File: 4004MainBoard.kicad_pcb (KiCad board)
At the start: 2 copper layers, 95.1 x 72.1 mm, 157 parts, among them J1 BUS, J2 P0 RAM1, J3 CMRAM RAM2, J4 P0 RAM2, J5 DC 5V, Q1 2SA1162GR, Q10 2SC2712GR, Q11 2SA1162GR, Q2 2SC2712GR, Q3 2SA1162GR, Q4 2SC2712GR, Q5 2SA1162GR, Q6 2SA1162GR, Q7 2SA1162GR, Q8 2SA1162GR, Q9 2SC2712GR, SW1 TEST, SW2 RESET, SW3 POWER, U1 74HC08, U2 74HC161, U3 PST600, U4 Intel4004, U5 LT1931A, U6 74LS540, U7 Intel4002-1, U8 Intel4002-1, U9 LT1763, Y1 DLO555MB

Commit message: migrate to KiCad 7
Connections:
- U1 pad 3: Net-(U1-Pad3) -> unconnected-(U1-Pad3)
- U1 pad 6: Net-(U1-Pad6) -> unconnected-(U1-Pad6)
- U2 pad 13: Net-(U2-Pad13) -> unconnected-(U2-Q1-Pad13)
- U2 pad 14: Net-(U2-Pad14) -> unconnected-(U2-Q0-Pad14)
- U2 pad 15: Net-(U2-Pad15) -> unconnected-(U2-Tc-Pad15)
- U2 pad 3: Net-(U2-Pad3) -> unconnected-(U2-P0-Pad3)
- U2 pad 4: Net-(U2-Pad4) -> unconnected-(U2-P1-Pad4)
- U2 pad 5: Net-(U2-Pad5) -> unconnected-(U2-P2-Pad5)
- U2 pad 6: Net-(U2-Pad6) -> unconnected-(U2-P3-Pad6)
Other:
- net class Default removed

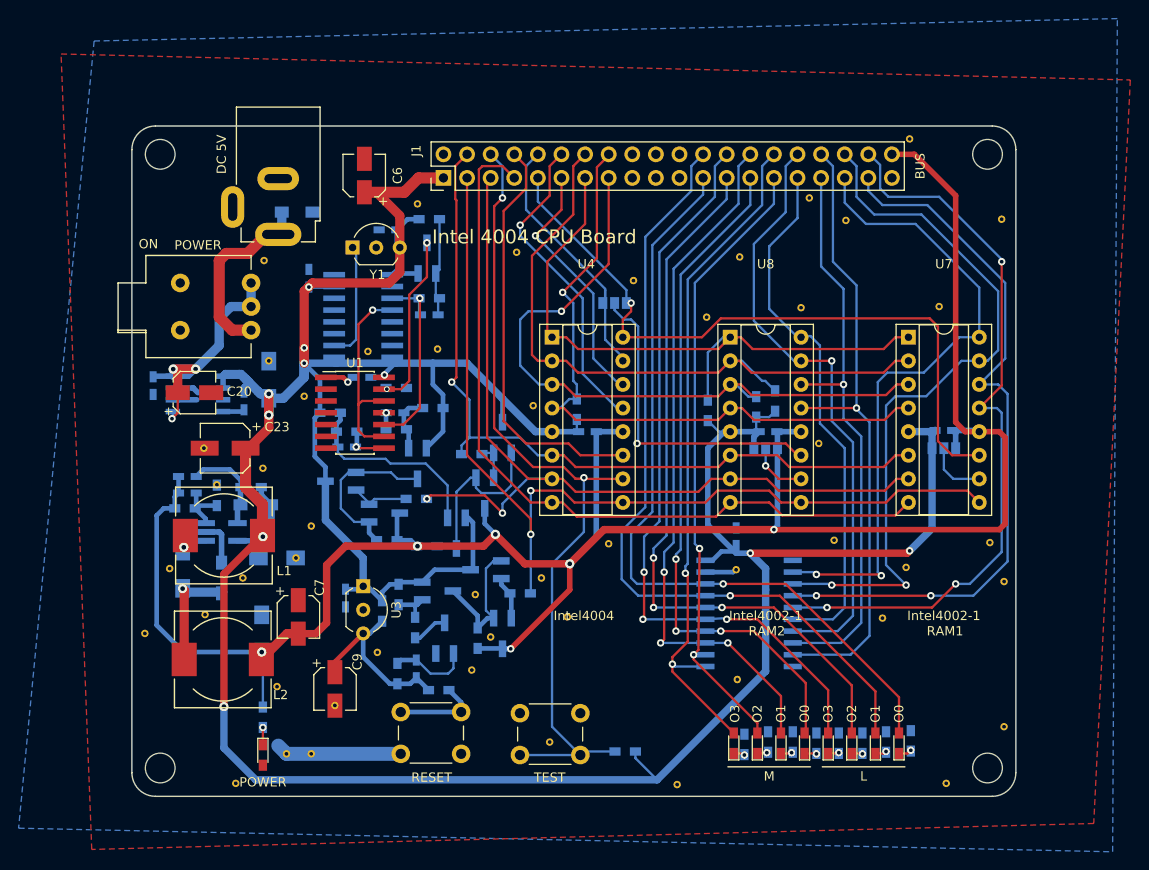
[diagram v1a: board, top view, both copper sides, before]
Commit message: update descrete buffer add notes
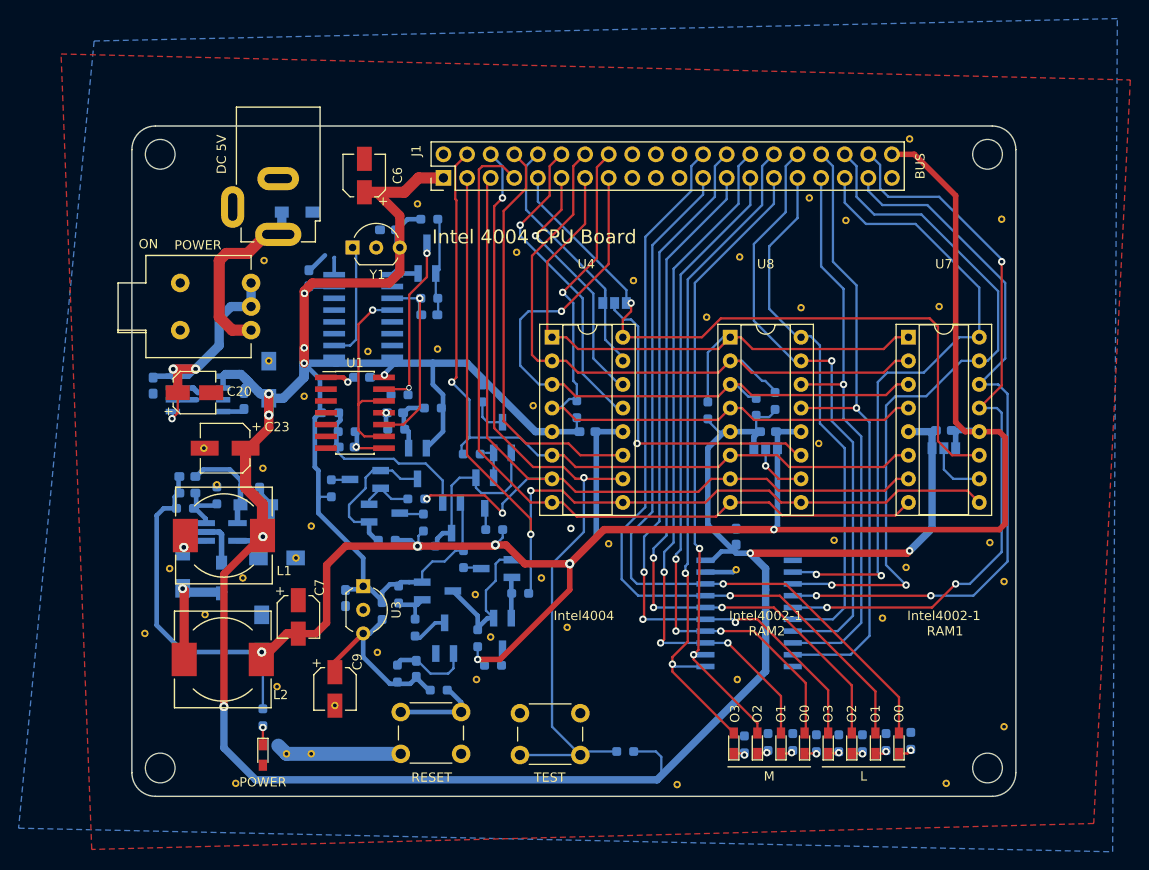
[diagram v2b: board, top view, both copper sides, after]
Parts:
- removed the REF** at (176.4, 137.4)
- added R36: 22, Resistor_SMD:R_0603_1608Metric_Pad0.98x0.95mm_HandSolder, B.Cu at (167.1, 117.7)
- added R37: 22, Resistor_SMD:R_0603_1608Metric_Pad0.98x0.95mm_HandSolder, B.Cu at (170.3, 129.2)
- added R38: 22, Resistor_SMD:R_0603_1608Metric_Pad0.98x0.95mm_HandSolder, B.Cu at (152.9, 110.1)
- added R39: 22, Resistor_SMD:R_0603_1608Metric_Pad0.98x0.95mm_HandSolder, B.Cu at (162.8, 113.8)
- added R40: 22, Resistor_SMD:R_0603_1608Metric_Pad0.98x0.95mm_HandSolder, B.Cu at (170.4, 114.6)
- added R41: 22, Resistor_SMD:R_0603_1608Metric_Pad0.98x0.95mm_HandSolder, B.Cu at (169.2, 99.9)
- C1, C12, C13, C15, C16, C17, C18, C19, C2, C21, C24, C25, C3, C4, C5, C8: footprint Capacitors_SMD:C_0603_HandSoldering -> Capacitor_SMD:C_0603_1608Metric_Pad1.08x0.95mm_HandSolder
- R1, R11, R2, R5, R9: value 300 -> 330; footprint Resistors_SMD:R_0603_HandSoldering -> Resistor_SMD:R_0603_1608Metric_Pad0.98x0.95mm_HandSolder
- R10, R12, R13, R15, R16, R17, R18, R19, R20, R21, R22, R23, R24, R25, R26, R27, R28, R29, R3, R30, R31, R32, R33, R34, R35, R4, R6, R7, R8: footprint Resistors_SMD:R_0603_HandSoldering -> Resistor_SMD:R_0603_1608Metric_Pad0.98x0.95mm_HandSolder
- R14: value 0 -> 1k; footprint Resistors_SMD:R_0603_HandSoldering -> Resistor_SMD:R_0603_1608Metric_Pad0.98x0.95mm_HandSolder
- moved Q2 2.65 mm to (156.6, 109.2)
- moved Q3 1.73 mm to (165.8, 113.3)
- moved Q9 1.15 mm to (170.7, 118.7)
- moved REF** 1.14 mm to (168.5, 130.7)
- moved REF** 1.12 mm to (178.3, 125.1)
- moved R9 0.82 mm to (160.2, 100.1), turned to 180 degrees
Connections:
- Q11 pad 3: /-10V -> Net-(Q11-C)
- Q2 pad 3: VCC -> Net-(Q2-C)
- Q4 pad 3: VCC -> Net-(Q4-C)
- Q5 pad 3: /-10V -> Net-(Q5-C)
- Q6 pad 3: /-10V -> Net-(Q6-C)
- Q9 pad 3: VCC -> Net-(Q9-C)
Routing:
- net GND: track 33.9 -> 38.1 mm, vias 1 -> 2
- net Net-(Q4-C): track 0.00 -> 4.02 mm
- net Net-(Q5-C): track 0.00 -> 2.58 mm
- net Net-(Q6-C): track 0.00 -> 2.33 mm
- net Net-(Q2-C): track 0.00 -> 2.03 mm
- net Net-(Q1-C): track 17.9 -> 15.9 mm
- net Net-(Q9-C): track 0.00 -> 1.95 mm
- net Net-(Q3-B): track 21.3 -> 19.4 mm
- net Net-(Q11-C): track 0.00 -> 1.82 mm
- net VCC: track 385.2 -> 386.5 mm
- net Net-(Q7-C): track 19.3 -> 20.3 mm
- net Net-(Q11-B): track 14.9 -> 15.8 mm
- net Net-(Q2-E): track 6.39 -> 5.64 mm
- net /-10V: track 238.4 -> 237.8 mm
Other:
- board text added: "2023-01-06"
- board text removed: "2018-05-13"
